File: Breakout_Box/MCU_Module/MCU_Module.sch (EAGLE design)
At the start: 18 parts, among them Q1 QUARZ5, U1 MIC5205-3.3, U2 MSP430G2553RHB32

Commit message: Licenses
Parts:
- renumbered SV3 to H1
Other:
- note added: "MCU Module for Nexus Project by Cycfi Research is licensed under a Creative Commons Attribution-ShareAlike 4.0 International License. Copyright CYCFI Research Inc. 2013-2016"
- note removed: "MCU Module Project by Cycfi Research is licensed under a Creative Commons Attribution 3.0 Unported License. http://creativecommons.org/licenses/by/3.0/deed.en_US Copyright CYCFI Research Inc. 2013-2016"

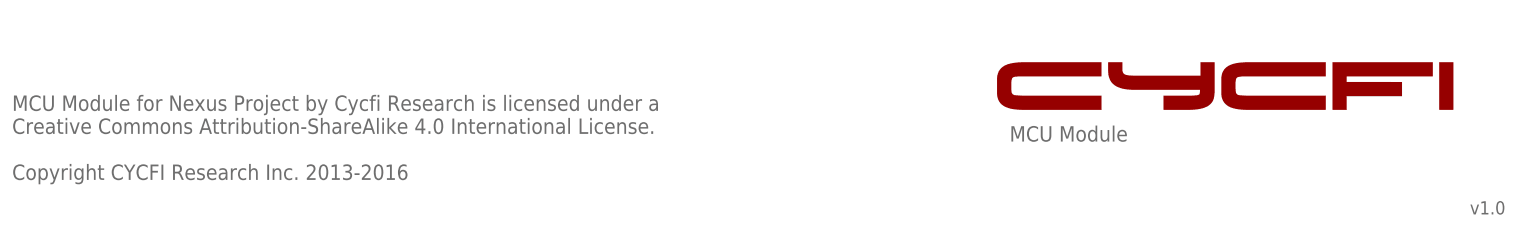
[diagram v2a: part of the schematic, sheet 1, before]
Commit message: Updated copyright and document number of schematics
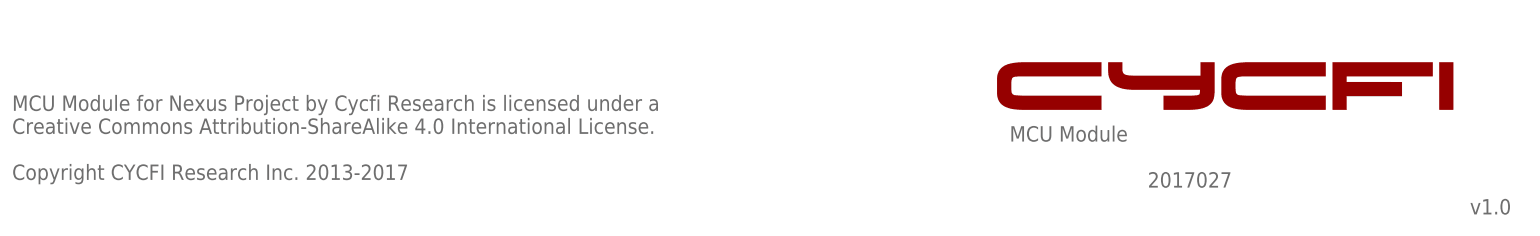
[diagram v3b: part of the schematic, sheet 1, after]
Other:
- note added: "2017027"
- note added: "MCU Module for Nexus Project by Cycfi Research is licensed under a Creative Commons Attribution-ShareAlike 4.0 International License. Copyright CYCFI Research Inc. 2013-2017"
- note removed: "MCU Module for Nexus Project by Cycfi Research is licensed under a Creative Commons Attribution-ShareAlike 4.0 International License. Copyright CYCFI Research Inc. 2013-2016"
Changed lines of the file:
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@@
 <?xml version="1.0" encoding="utf-8"?>
 <!DOCTYPE eagle SYSTEM "eagle.dtd">
-<eagle version="6.3">
+<eagle version="7.6.0">
 <drawing>
 <settings>
@@
 <text x="87.63" y="156.21" size="1.778" layer="95">3.3V</text>
 <text x="177.8" y="19.05" size="2.54" layer="95">MCU Module</text>
-<text x="254" y="6.985" size="2.1844" layer="95">v1.0</text>
+<text x="254" y="6.985" size="2.54" layer="95">v1.0</text>
 <text x="12.7" y="12.7" size="2.54" layer="95">MCU Module for Nexus Project by Cycfi Research is licensed under a
 Creative Commons Attribution-ShareAlike 4.0 International License.
-Copyright CYCFI Research Inc. 2013-2016</text>
+Copyright CYCFI Research Inc. 2013-2017</text>
 <rectangle x1="179.80469375" y1="24.29065625" x2="193.0330125" y2="24.29954375" layer="94"/>
 <rectangle x1="203.283184375" y1="24.29065625" x2="207.683734375" y2="24.29954375" layer="94"/>
@@
 <rectangle x1="231.251125" y1="32.176084375" x2="247.86653125" y2="32.184971875" layer="94"/>
 <rectangle x1="248.915553125" y1="32.176084375" x2="251.271403125" y2="32.184971875" layer="94"/>
+<text x="200.66" y="11.43" size="2.54" layer="95">2017027</text>
 </plain>
 <instances>

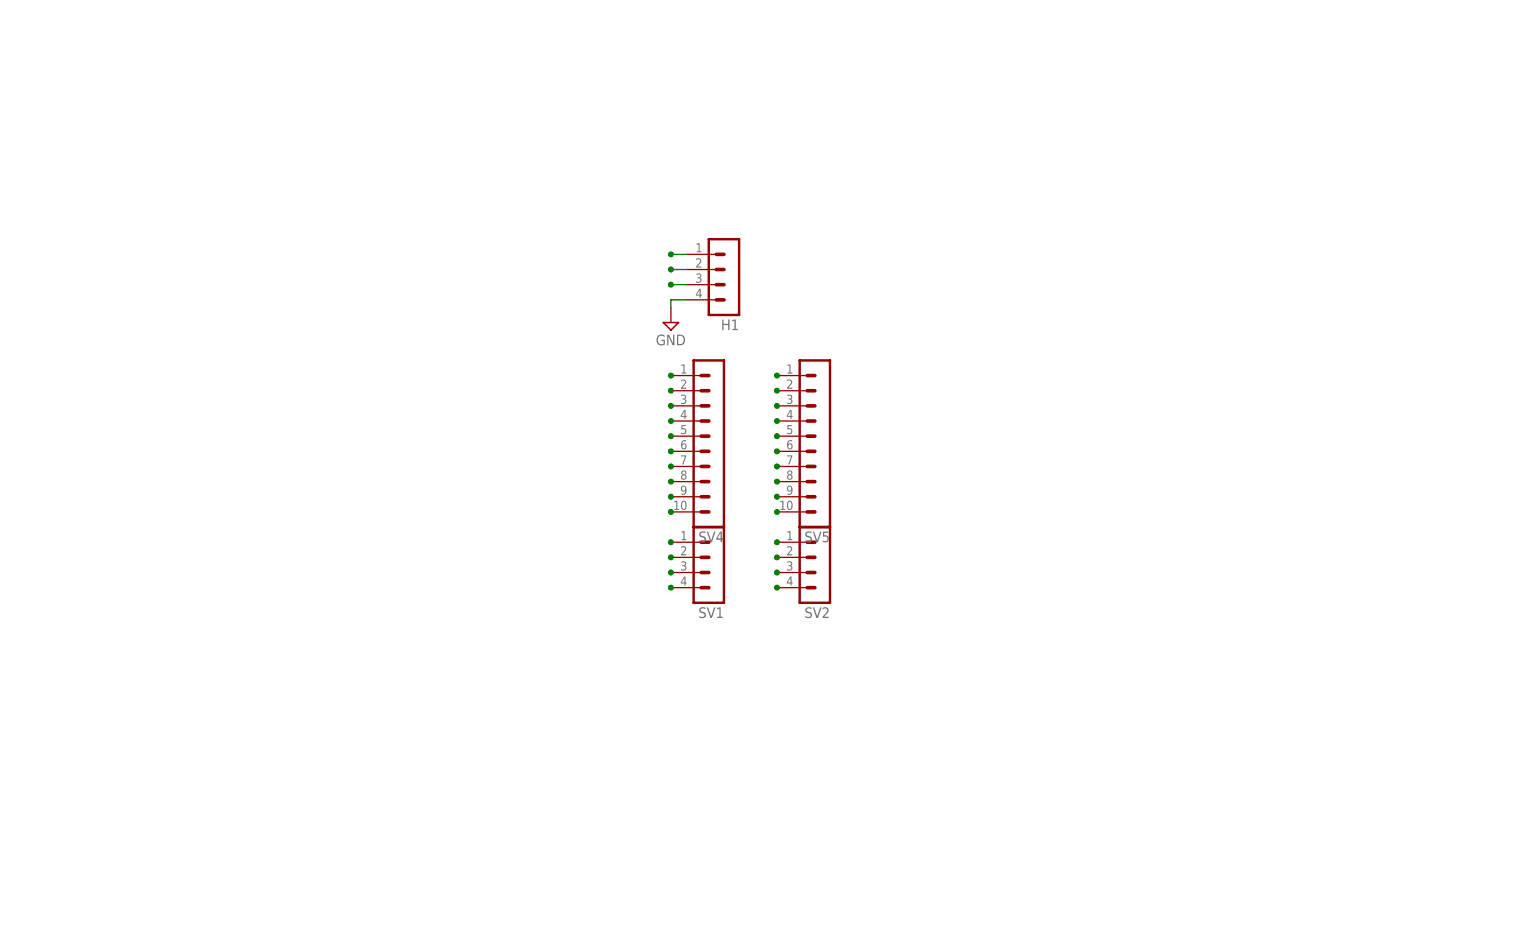
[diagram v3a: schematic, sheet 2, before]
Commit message: Update: Main Board MIDI Board MCU Board IO Board
Delete:
Mixer Board
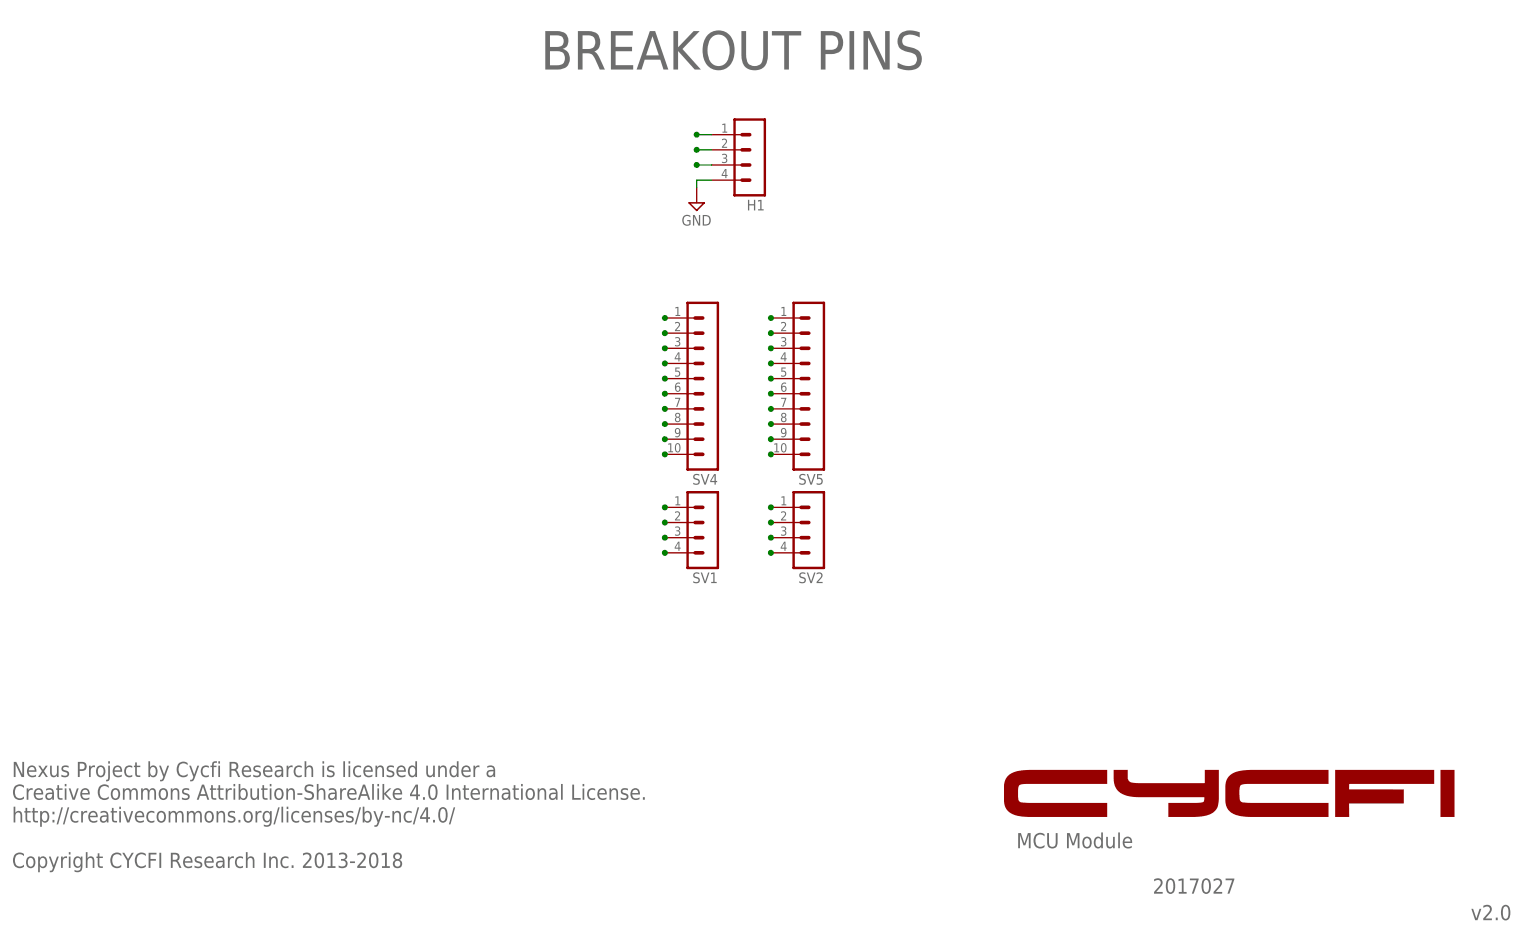
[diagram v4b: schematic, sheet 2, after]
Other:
- note added: "BREAKOUT PINS"
- note added: "Nexus Project by Cycfi Research is licensed under a Creative Commons Attribution-ShareAlike 4.0 International License. http://creativecommons.org/licenses/by-nc/4.0/ Copyright CYCFI Research Inc. 2013-2018"
- note added: "P1.0"
- note added: "P1.1"
- note added: "P1.2"
- note added: "P1.3"
- note added: "P1.4"
- note added: "P1.5"
- note added: "P1.6"
- note added: "P1.7"
- note added: "P2.0"
- note added: "P2.1"
- note added: "P2.2"
- note added: "P2.3"
- note added: "P2.4"
- note added: "P2.5"
- note added: "P2.6"
- note added: "P2.7"
- note added: "P3.0"
- note added: "P3.1"
- note added: "P3.2"
- note added: "P3.3"
- note added: "P3.4"
- note added: "P3.5"
- note added: "P3.6"
- note added: "P3.7"
- note added: "v2.0"
- note removed: "MCU Module for Nexus Project by Cycfi Research is licensed under a Creative Commons Attribution-ShareAlike 4.0 International License. Copyright CYCFI Research Inc. 2013-2017"
- note removed: "v1.0"
- moved on the sheet: H1, SV1, SV2, SV4, SV5

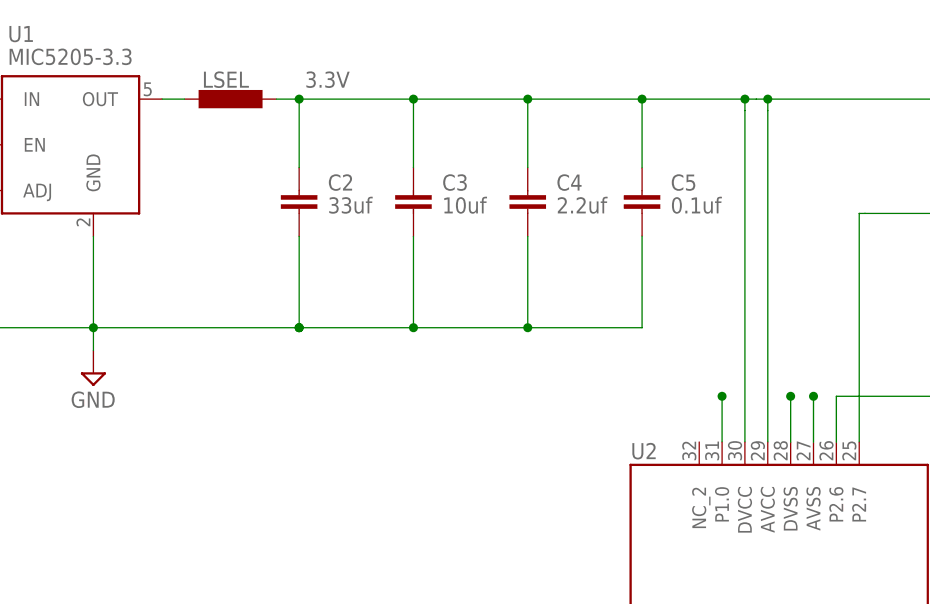
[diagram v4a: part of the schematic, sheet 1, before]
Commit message: Slight Changes to MIDI and MCU: - Change BJT Part number on MIDI_Module - Delete Ferrite Bead on MCU_Module
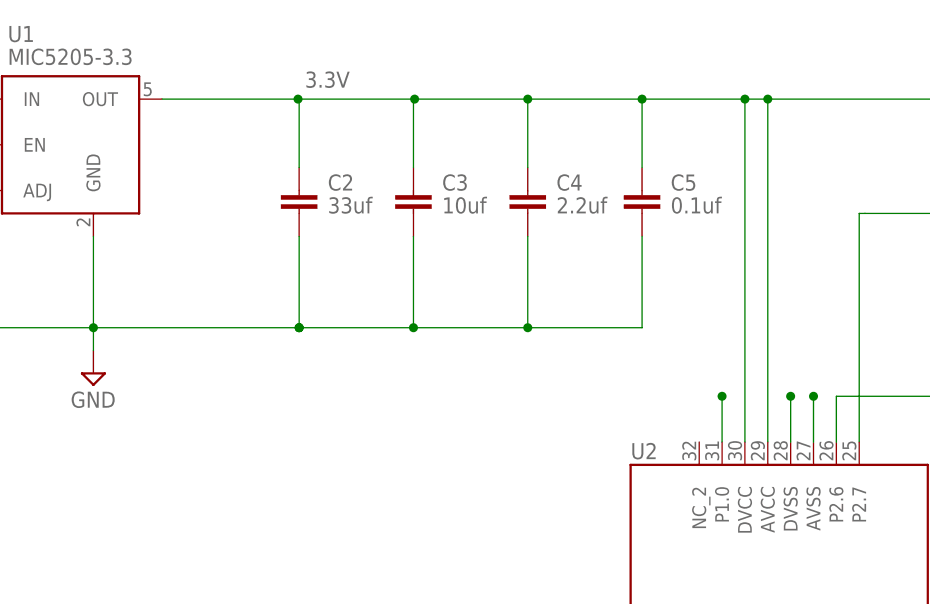
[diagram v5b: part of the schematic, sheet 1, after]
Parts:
- removed LSEL: FERRITE_BEAD, Cycfi:FERRITE_BEAD
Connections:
- removed net N$1: LSEL.1, U1.OUT
- net DVCC(3.3V): now also U1.OUT; no longer LSEL.2
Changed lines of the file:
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@@
 <part name="P+1" library="supply1" deviceset="VCC" device=""/>
 <part name="R1" library="resistor" deviceset="R-EU_" device="R0402" value="47K"/>
-<part name="LSEL" library="Cycfi" deviceset="FERRITE_BEAD" device="" value=""/>
 <part name="C6" library="resistor" deviceset="C-EU" device="C0603" value="1nf"/>
 <part name="C1" library="resistor" deviceset="C-EU" device="C0805" value="1uf"/>
@@
 <attribute name="VALUE" x="179.07" y="99.06" size="1.778" layer="96"/>
 </instance>
-<instance part="LSEL" gate="G$1" x="79.375" y="154.94" smashed="yes" rot="R90">
-<attribute name="NAME" x="76.2" y="156.21" size="1.778" layer="95"/>
-<attribute name="VALUE" x="83.185" y="158.242" size="1.778" layer="96" rot="R180"/>
-</instance>
 <instance part="C6" gate="G$1" x="177.165" y="88.9" smashed="yes">
 <attribute name="NAME" x="180.34" y="87.63" size="1.778" layer="95"/>
@@
 <segment>
 <pinref part="U2" gate="G$1" pin="DVCC"/>
-<wire x1="136.525" y1="116.84" x2="136.525" y2="153.67" width="0.1524" layer="91"/>
+<wire x1="136.525" y1="116.84" x2="136.525" y2="154.94" width="0.1524" layer="91"/>
 <pinref part="R1" gate="G$1" pin="1"/>
 <wire x1="177.165" y1="106.68" x2="177.165" y2="154.94" width="0.1524" layer="91"/>
 <wire x1="177.165" y1="154.94" x2="139.065" y2="154.94" width="0.1524" layer="91"/>
-<wire x1="139.065" y1="154.94" x2="137.795" y2="154.94" width="0.1524" layer="91"/>
 <pinref part="U2" gate="G$1" pin="AVCC"/>
-<wire x1="139.065" y1="116.84" x2="139.065" y2="153.67" width="0.1524" layer="91"/>
+<wire x1="139.065" y1="116.84" x2="139.065" y2="154.94" width="0.1524" layer="91"/>
 <pinref part="C4" gate="G$1" pin="1"/>
 <wire x1="112.395" y1="147.32" x2="112.395" y2="154.94" width="0.1524" layer="91"/>
@@
 <pinref part="C3" gate="G$1" pin="1"/>
 <wire x1="99.695" y1="147.32" x2="99.695" y2="154.94" width="0.1524" layer="91"/>
-<junction x="99.695" y="154.94"/>
-<wire x1="99.695" y1="154.94" x2="112.395" y2="154.94" width="0.1524" layer="91"/>
-<wire x1="86.995" y1="154.94" x2="99.695" y2="154.94" width="0.1524" layer="91"/>
-<pinref part="LSEL" gate="G$1" pin="2"/>
-<wire x1="84.455" y1="154.94" x2="86.995" y2="154.94" width="0.1524" layer="91"/>
-<junction x="86.995" y="154.94"/>
-<wire x1="86.995" y1="154.94" x2="86.995" y2="147.32" width="0.1524" layer="91"/>
-<pinref part="C2" gate="G$1" pin="1"/>
-<wire x1="137.795" y1="154.94" x2="136.525" y2="154.94" width="0.1524" layer="91"/>
+<wire x1="99.695" y1="154.94" x2="99.822" y2="154.94" width="0.1524" layer="91"/>
+<wire x1="99.822" y1="154.94" x2="112.395" y2="154.94" width="0.1524" layer="91"/>
+<wire x1="139.065" y1="154.94" x2="136.525" y2="154.94" width="0.1524" layer="91"/>
 <junction x="125.095" y="154.94"/>
 <wire x1="136.525" y1="154.94" x2="125.095" y2="154.94" width="0.1524" layer="91"/>
-<wire x1="136.525" y1="153.67" x2="136.525" y2="154.94" width="0.1524" layer="91"/>
-<wire x1="139.065" y1="153.67" x2="139.065" y2="154.94" width="0.1524" layer="91"/>
 <junction x="136.525" y="154.94"/>
 <junction x="139.065" y="154.94"/>
+<pinref part="U1" gate="G1" pin="OUT"/>
+<wire x1="71.755" y1="154.94" x2="86.868" y2="154.94" width="0.1524" layer="91"/>
+<pinref part="C2" gate="G$1" pin="1"/>
+<wire x1="86.995" y1="154.94" x2="99.695" y2="154.94" width="0.1524" layer="91"/>
+<wire x1="86.995" y1="147.32" x2="86.995" y2="154.94" width="0.1524" layer="91"/>
+<wire x1="86.995" y1="154.94" x2="86.868" y2="154.94" width="0.1524" layer="91"/>
+<junction x="86.868" y="154.94"/>
+<junction x="99.822" y="154.94"/>
 </segment>
 </net>
@@
 </segment>
 </net>
-<net name="N$1" class="0">
-<segment>
-<pinref part="U1" gate="G1" pin="OUT"/>
-<wire x1="74.295" y1="154.94" x2="71.755" y2="154.94" width="0.1524" layer="91"/>
-<pinref part="LSEL" gate="G$1" pin="1"/>
-</segment>
-</net>
